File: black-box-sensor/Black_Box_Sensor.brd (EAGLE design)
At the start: 37.2 x 44 mm, 59 parts, among them J1 104031-0811, J2 UX60-MB-5S8, J3 B4B-PH-SM4-TBT(LF)(SN), U1 ADXL375, U2 ADXL375, U3 ATMEGA32U4-AU, U4 FXAS21002CQR1, U5 IAM-20380, U6 NL27WZ32USG, U7 LT1129CST-5#PBF, U8 AD8426ACPZ-WP, U9 TXU0304

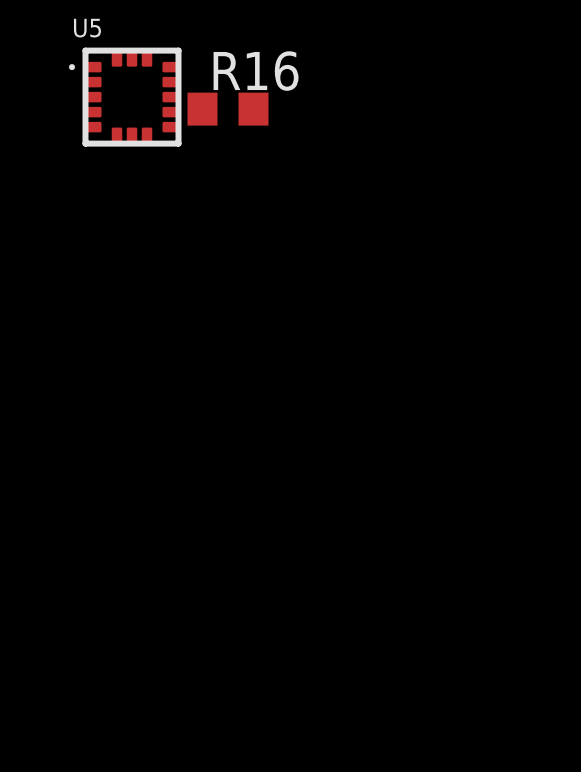
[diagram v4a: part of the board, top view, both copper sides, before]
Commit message: Added gyroscope
missing some connections, and its capacitors may not have the right footprint, will follow up with Valentin later about it
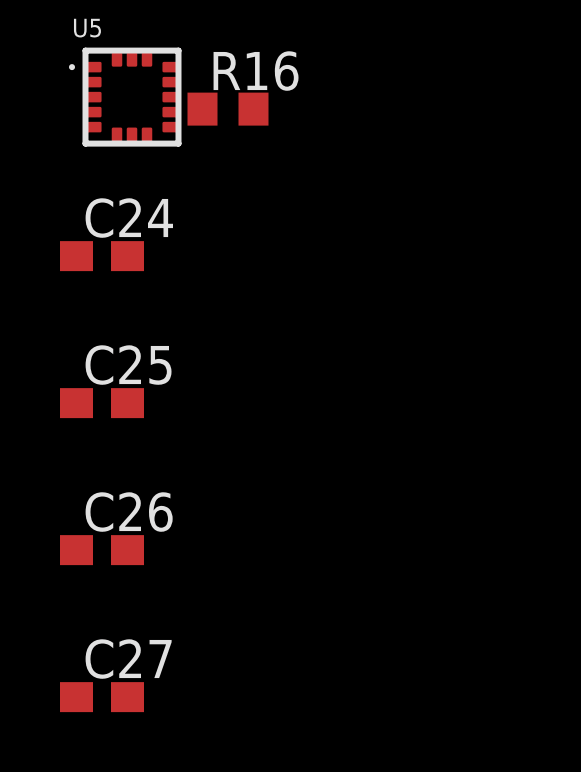
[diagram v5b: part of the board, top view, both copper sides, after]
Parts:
- added C24: 0.1uF, rcl:C0603
- added C25: 2.2uF, rcl:C0603
- added C26: 0.47uF, rcl:C0603
- added C27: 10nF, rcl:C0603
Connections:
- new net N$10: C26.1, U5.14
- net 3.3V: now also C24.1, C25.1, C27.1, U5.1, U5.16, U5.5
- net GND: now also C24.2, C25.2, C26.2, C27.2, U5.10, U5.11, U5.12, U5.13, U5.15, U5.9
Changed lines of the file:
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@@
 <?xml version="1.0" encoding="utf-8"?>
 <!DOCTYPE eagle SYSTEM "eagle.dtd">
-<eagle version="9.6.2">
+<eagle version="9.5.1">
 <drawing>
 <settings>
@@
 <attribute name="VALUE" x="-3.8" y="-12.7" size="0.609659375" layer="27" font="vector" ratio="10" align="top-left"/>
 </element>
+<element name="C24" library="rcl" library_urn="urn:adsk.eagle:library:334" package="C0603" package3d_urn="urn:adsk.eagle:package:23616/2" value="0.1uF" x="-2.8" y="-16" smashed="yes">
+<attribute name="DKPN" value="CGA3E2X7R1E104K080AA " x="-2.8" y="-16" size="1.778" layer="27" display="off"/>
+<attribute name="NAME" x="-3.435" y="-15.365" size="1.27" layer="25"/>
+<attribute name="POPULARITY" value="37" x="-2.8" y="-16" size="1.778" layer="27" display="off"/>
+<attribute name="SPICEPREFIX" value="C" x="-2.8" y="-16" size="1.778" layer="27" display="off"/>
+<attribute name="VALUE" x="-3.435" y="-17.905" size="1.27" layer="27"/>
+</element>
+<element name="C25" library="rcl" library_urn="urn:adsk.eagle:library:334" package="C0603" package3d_urn="urn:adsk.eagle:package:23616/2" value="2.2uF" x="-2.8" y="-20.9" smashed="yes">
+<attribute name="DKPN" value="C1608X5R1C225K080AB" x="-2.8" y="-20.9" size="1.778" layer="27" display="off"/>
+<attribute name="NAME" x="-3.435" y="-20.265" size="1.27" layer="25"/>
+<attribute name="POPULARITY" value="37" x="-2.8" y="-20.9" size="1.778" layer="27" display="off"/>
+<attribute name="SPICEPREFIX" value="C" x="-2.8" y="-20.9" size="1.778" layer="27" display="off"/>
+<attribute name="VALUE" x="-3.435" y="-22.805" size="1.27" layer="27"/>
+</element>
+<element name="C26" library="rcl" library_urn="urn:adsk.eagle:library:334" package="C0603" package3d_urn="urn:adsk.eagle:package:23616/2" value="0.47uF" x="-2.8" y="-25.8" smashed="yes">
+<attribute name="DKPN" value="C0603X5R0J474M030BC" x="-2.8" y="-25.8" size="1.778" layer="27" display="off"/>
+<attribute name="NAME" x="-3.435" y="-25.165" size="1.27" layer="25"/>
+<attribute name="POPULARITY" value="37" x="-2.8" y="-25.8" size="1.778" layer="27" display="off"/>
+<attribute name="SPICEPREFIX" value="C" x="-2.8" y="-25.8" size="1.778" layer="27" display="off"/>
+<attribute name="VALUE" x="-3.435" y="-27.705" size="1.27" layer="27"/>
+</element>
+<element name="C27" library="rcl" library_urn="urn:adsk.eagle:library:334" package="C0603" package3d_urn="urn:adsk.eagle:package:23616/2" value="10nF" x="-2.8" y="-30.7" smashed="yes">
+<attribute name="DKPN" value="C1608X7R2A103M080AA" x="-2.8" y="-30.7" size="1.778" layer="27" display="off"/>
+<attribute name="NAME" x="-3.435" y="-30.065" size="1.27" layer="25"/>
+<attribute name="POPULARITY" value="37" x="-2.8" y="-30.7" size="1.778" layer="27" display="off"/>
+<attribute name="SPICEPREFIX" value="C" x="-2.8" y="-30.7" size="1.778" layer="27" display="off"/>
+<attribute name="VALUE" x="-3.435" y="-32.605" size="1.27" layer="27"/>
+</element>
 </elements>
 <signals>
@@
 <contactref element="C22" pad="2"/>
 <contactref element="C23" pad="2"/>
+<contactref element="U5" pad="9"/>
+<contactref element="U5" pad="13"/>
+<contactref element="U5" pad="15"/>
+<contactref element="U5" pad="11"/>
+<contactref element="U5" pad="12"/>
+<contactref element="U5" pad="10"/>
+<contactref element="C25" pad="2"/>
+<contactref element="C24" pad="2"/>
+<contactref element="C26" pad="2"/>
+<contactref element="C27" pad="2"/>
 <wire x1="35.6" y1="31.2314" x2="34.85" y2="32.5" width="0" layer="19" extent="16-16"/>
 <wire x1="33.06" y1="29.5" x2="35.3" y2="29.6" width="0" layer="19" extent="1-16"/>
@@
 <wire x1="21.98" y1="5.9352" x2="19.58" y2="3.6852" width="0" layer="19" extent="1-1"/>
 <wire x1="30.38" y1="3.6852" x2="21.98" y2="5.9352" width="0" layer="19" extent="1-1"/>
+<wire x1="-0.54" y1="-9.7" x2="4.6" y2="1.6" width="0" layer="19" extent="1-1"/>
+<wire x1="-0.54" y1="-10.2" x2="-0.54" y2="-9.7" width="0" layer="19" extent="1-1"/>
+<wire x1="-0.54" y1="-10.7" x2="-0.54" y2="-10.2" width="0" layer="19" extent="1-1"/>
+<wire x1="-0.54" y1="-11.2" x2="-0.54" y2="-10.7" width="0" layer="19" extent="1-1"/>
+<wire x1="-0.54" y1="-11.7" x2="-0.54" y2="-11.2" width="0" layer="19" extent="1-1"/>
+<wire x1="-1.8" y1="-9.44" x2="-0.54" y2="-9.7" width="0" layer="19" extent="1-1"/>
+<wire x1="-1.95" y1="-16" x2="-0.54" y2="-11.7" width="0" layer="19" extent="1-1"/>
+<wire x1="-1.95" y1="-20.9" x2="-1.95" y2="-16" width="0" layer="19" extent="1-1"/>
+<wire x1="-1.95" y1="-25.8" x2="-1.95" y2="-20.9" width="0" layer="19" extent="1-1"/>
+<wire x1="-1.95" y1="-30.7" x2="-1.95" y2="-25.8" width="0" layer="19" extent="1-1"/>
 </signal>
 <signal name="VBATT">
@@
 <contactref element="C22" pad="1"/>
 <contactref element="U$1" pad="5"/>
+<contactref element="C24" pad="1"/>
+<contactref element="C25" pad="1"/>
+<contactref element="U5" pad="16"/>
+<contactref element="C27" pad="1"/>
+<contactref element="U5" pad="1"/>
+<contactref element="U5" pad="5"/>
 <wire x1="25.96" y1="20.87" x2="29.48" y2="20.87" width="0" layer="19" extent="16-16"/>
 <wire x1="23.35" y1="17.965" x2="25.227775" y2="18.527775" width="0" layer="19" extent="1-1"/>
@@
 <wire x1="14.4" y1="34.75" x2="14.75" y2="35.1" width="0" layer="19" extent="1-16"/>
 <wire x1="11.335" y1="1.23" x2="11.04" y2="14.29" width="0" layer="19" extent="1-16"/>
+<wire x1="-2.3" y1="-9.44" x2="11.335" y2="1.23" width="0" layer="19" extent="1-1"/>
+<wire x1="-3.06" y1="-9.7" x2="-2.3" y2="-9.44" width="0" layer="19" extent="1-1"/>
+<wire x1="-3.06" y1="-11.7" x2="-3.06" y2="-9.7" width="0" layer="19" extent="1-1"/>
+<wire x1="-3.65" y1="-16" x2="-3.06" y2="-11.7" width="0" layer="19" extent="1-1"/>
+<wire x1="-3.65" y1="-20.9" x2="-3.65" y2="-16" width="0" layer="19" extent="1-1"/>
+<wire x1="-3.65" y1="-30.7" x2="-3.65" y2="-20.9" width="0" layer="19" extent="1-1"/>
 </signal>
 <signal name="N$1">
@@
 <contactref element="ISP1" pad="2"/>
 </signal>
+<signal name="N$10">
+<contactref element="U5" pad="14"/>
+<contactref element="C26" pad="1"/>
+<wire x1="-1.3" y1="-9.44" x2="-3.65" y2="-25.8" width="0" layer="19" extent="1-1"/>
+</signal>
 </signals>

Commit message: Gyroscope wiring complete
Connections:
- new net FSYNC_GYRO: U3.28
- new net INT6: U3.1
- new net N$11: U5.6
- new net N$12: U5.8
- net GND: now also U5.4
- net INT0: now also U5.2
- net INT1: now also U5.3
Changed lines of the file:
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@@
 <contactref element="C26" pad="2"/>
 <contactref element="C27" pad="2"/>
+<contactref element="U5" pad="4"/>
 <wire x1="35.6" y1="31.2314" x2="34.85" y2="32.5" width="0" layer="19" extent="16-16"/>
 <wire x1="33.06" y1="29.5" x2="35.3" y2="29.6" width="0" layer="19" extent="1-16"/>
@@
 <wire x1="-0.54" y1="-11.7" x2="-0.54" y2="-11.2" width="0" layer="19" extent="1-1"/>
 <wire x1="-1.8" y1="-9.44" x2="-0.54" y2="-9.7" width="0" layer="19" extent="1-1"/>
+<wire x1="-3.06" y1="-11.2" x2="-1.8" y2="-9.44" width="0" layer="19" extent="1-1"/>
 <wire x1="-1.95" y1="-16" x2="-0.54" y2="-11.7" width="0" layer="19" extent="1-1"/>
 <wire x1="-1.95" y1="-20.9" x2="-1.95" y2="-16" width="0" layer="19" extent="1-1"/>
@@
 <wire x1="22.8" y1="24.5" x2="22.498" y2="24.198" width="0.2" layer="1"/>
 <wire x1="22.498" y1="24.198" x2="20.629775" y2="24.198" width="0.2" layer="1"/>
+<contactref element="U5" pad="3"/>
+<wire x1="-3.06" y1="-10.7" x2="6.94" y2="24.8475" width="0" layer="19" extent="1-1"/>
 </signal>
 <signal name="INT0">
@@
 <wire x1="8.7" y1="24.9" x2="8.6475" y2="24.8475" width="0.2" layer="1"/>
 <wire x1="8.6475" y1="24.8475" x2="7.74" y2="24.8475" width="0.2" layer="1"/>
+<contactref element="U5" pad="2"/>
+<wire x1="-3.06" y1="-10.2" x2="7.74" y2="24.8475" width="0" layer="19" extent="1-1"/>
 </signal>
 <signal name="CURRENT">
@@
 <wire x1="-1.3" y1="-9.44" x2="-3.65" y2="-25.8" width="0" layer="19" extent="1-1"/>
 </signal>
+<signal name="INT6">
+<contactref element="U3" pad="1"/>
+</signal>
+<signal name="N$11">
+<contactref element="U5" pad="6"/>
+</signal>
+<signal name="FSYNC_GYRO">
+<contactref element="U3" pad="28"/>
+</signal>
+<signal name="N$12">
+<contactref element="U5" pad="8"/>
+</signal>
 </signals>

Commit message: clean schematic for DR
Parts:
- removed C11, C12: 0.1uF, rcl:C0603K
- removed C6: 0.1uF, rcl:C0603
- removed U4: FXAS21002CQR1, BBS_Library:24-TFQFN
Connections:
- removed net FSYNC_GYRO: U3.28
- removed net N$1: C6.1, U4.16
- removed net N$11: U5.6
- removed net N$12: U5.8
- new net FSYNC: U3.28, U5.8
- net 3.3V: no longer C11.1, C12.1, U4.15, U4.18, U4.4, U4.8
- net CS3: no longer U4.17
- net GND: no longer C11.2, C12.2, C6.2, U4.1, U4.10, U4.14, U4.19, U4.20, U4.21, U4.22, U4.23, U4.24, U4.5, U4.6, U4.7, U4.9
- net INT6: now also U5.6
- net MISO: no longer U4.13
- net MOSI: no longer U4.12
- net SCLK: no longer U4.11
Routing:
- net GND: track 82.3 -> 66.4 mm, vias 31 -> 24
- net 3.3V: track 46.5 -> 40.4 mm, vias 13 -> 11
- net N$1: track 2.75 -> 0.00 mm, vias 1 -> 0
- net SCLK: track 53.0 -> 51.9 mm
- net MOSI: track 34.6 -> 33.6 mm

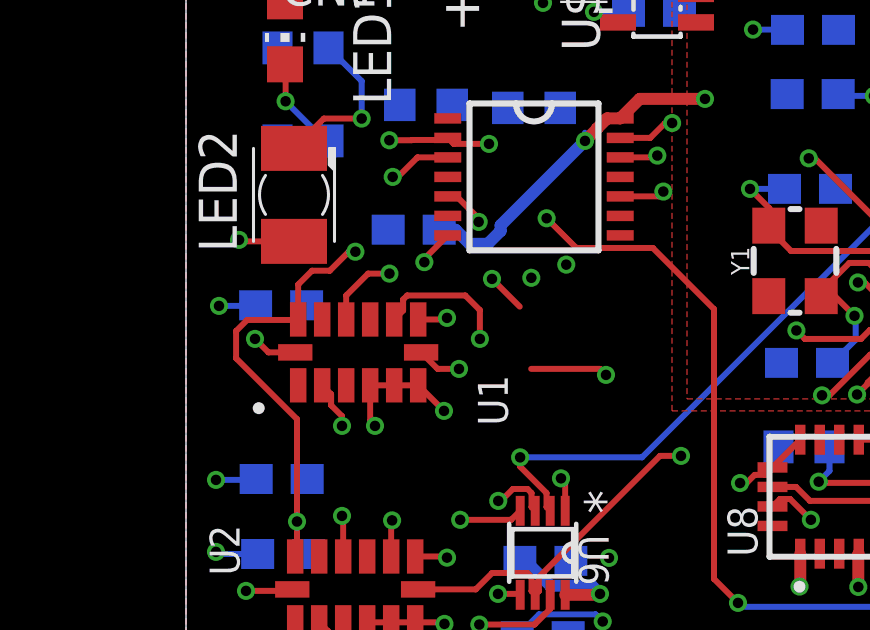
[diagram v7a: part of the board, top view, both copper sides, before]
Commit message: fix some pin connections, but possibly will switch microcontroller
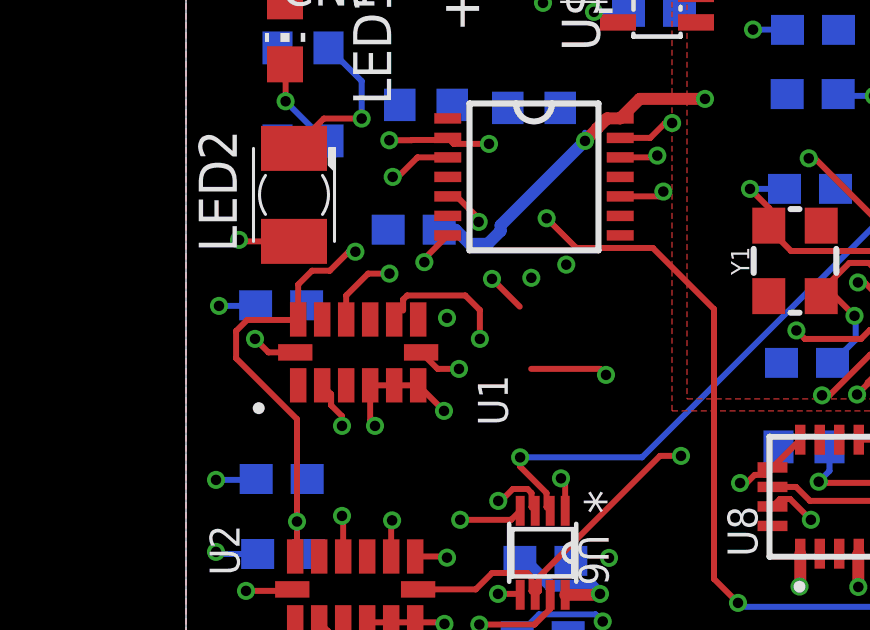
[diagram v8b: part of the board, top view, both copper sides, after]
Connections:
- new net SCL: U3.18, U5.2
- new net SDA: U3.19, U5.3
- net INT0: now also U3.29; no longer U3.18, U5.2
- net INT1: now also U3.30; no longer U3.19, U5.3
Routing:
- net INT1: track 19.4 -> 0.00 mm, vias 2 -> 0
- net SDA: track 0.00 -> 19.0 mm, vias 0 -> 2
- net INT0: track 17.0 -> 0.00 mm, vias 2 -> 0
- net SCL: track 0.00 -> 16.1 mm, vias 0 -> 2
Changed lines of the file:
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@@
 <wire x1="23.178975" y1="23.2" x2="23.7" y2="23.2" width="0.2" layer="1"/>
 </signal>
-<signal name="INT1">
+<signal name="SDA">
 <contactref element="U3" pad="19"/>
-<contactref element="U1" pad="9"/>
 <via x="9.7964" y="24.2" extent="1-16" drill="0.35"/>
 <wire x1="7.238" y1="25.514025" x2="7.370975" y2="25.647" width="0.2" layer="1"/>
 <wire x1="7.370975" y1="25.647" x2="9.309025" y2="25.647" width="0.2" layer="1"/>
-<wire x1="6.94" y1="24.8475" x2="7.238" y2="25.1455" width="0.2" layer="1"/>
 <wire x1="7.238" y1="25.1455" x2="7.238" y2="25.514025" width="0.2" layer="1"/>
 <wire x1="9.7964" y1="24.2" x2="9.7964" y2="25.159625" width="0.2" layer="1"/>
@@
 <wire x1="22.498" y1="24.198" x2="20.629775" y2="24.198" width="0.2" layer="1"/>
 <contactref element="U5" pad="3"/>
-<wire x1="-3.06" y1="-10.7" x2="6.94" y2="24.8475" width="0" layer="19" extent="1-1"/>
-</signal>
-<signal name="INT0">
+<wire x1="-3.06" y1="-10.7" x2="9.7964" y2="24.2" width="0" layer="19" extent="1-1"/>
+</signal>
+<signal name="SCL">
 <contactref element="U3" pad="18"/>
-<contactref element="U1" pad="8"/>
 <via x="22.3988875" y="26.0811125" extent="1-16" drill="0.35"/>
 <wire x1="23.7" y1="25.6" x2="23.101025" y2="25.6" width="0.2" layer="1"/>
@@
 <wire x1="10.42499375" y1="25.3204" x2="10.00459375" y2="24.9" width="0.2" layer="15"/>
 <wire x1="8.7" y1="24.9" x2="8.6475" y2="24.8475" width="0.2" layer="1"/>
-<wire x1="8.6475" y1="24.8475" x2="7.74" y2="24.8475" width="0.2" layer="1"/>
 <contactref element="U5" pad="2"/>
-<wire x1="-3.06" y1="-10.2" x2="7.74" y2="24.8475" width="0" layer="19" extent="1-1"/>
+<wire x1="-3.06" y1="-10.2" x2="8.6475" y2="24.8475" width="0" layer="19" extent="1-1"/>
 </signal>
 <signal name="CURRENT">
@@
 <wire x1="-1.3" y1="-11.96" x2="29.5" y2="20.6" width="0" layer="19" extent="1-1"/>
 </signal>
+<signal name="INT0">
+<contactref element="U1" pad="8"/>
+<contactref element="U3" pad="29"/>
+<wire x1="7.74" y1="24.8475" x2="30.3" y2="20.6" width="0" layer="19" extent="1-1"/>
+</signal>
+<signal name="INT1">
+<contactref element="U1" pad="9"/>
+<contactref element="U3" pad="30"/>
+<wire x1="6.94" y1="24.8475" x2="31.1" y2="20.6" width="0" layer="19" extent="1-1"/>
+</signal>
 </signals>
